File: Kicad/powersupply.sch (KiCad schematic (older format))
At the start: 18 parts, among them J1701 Jack-DC, Q1701 BC546, Q1702 BC556, U1701 DC-DC Module, U1702 MAX1615, U1703 TLV1117 3.3V 1A

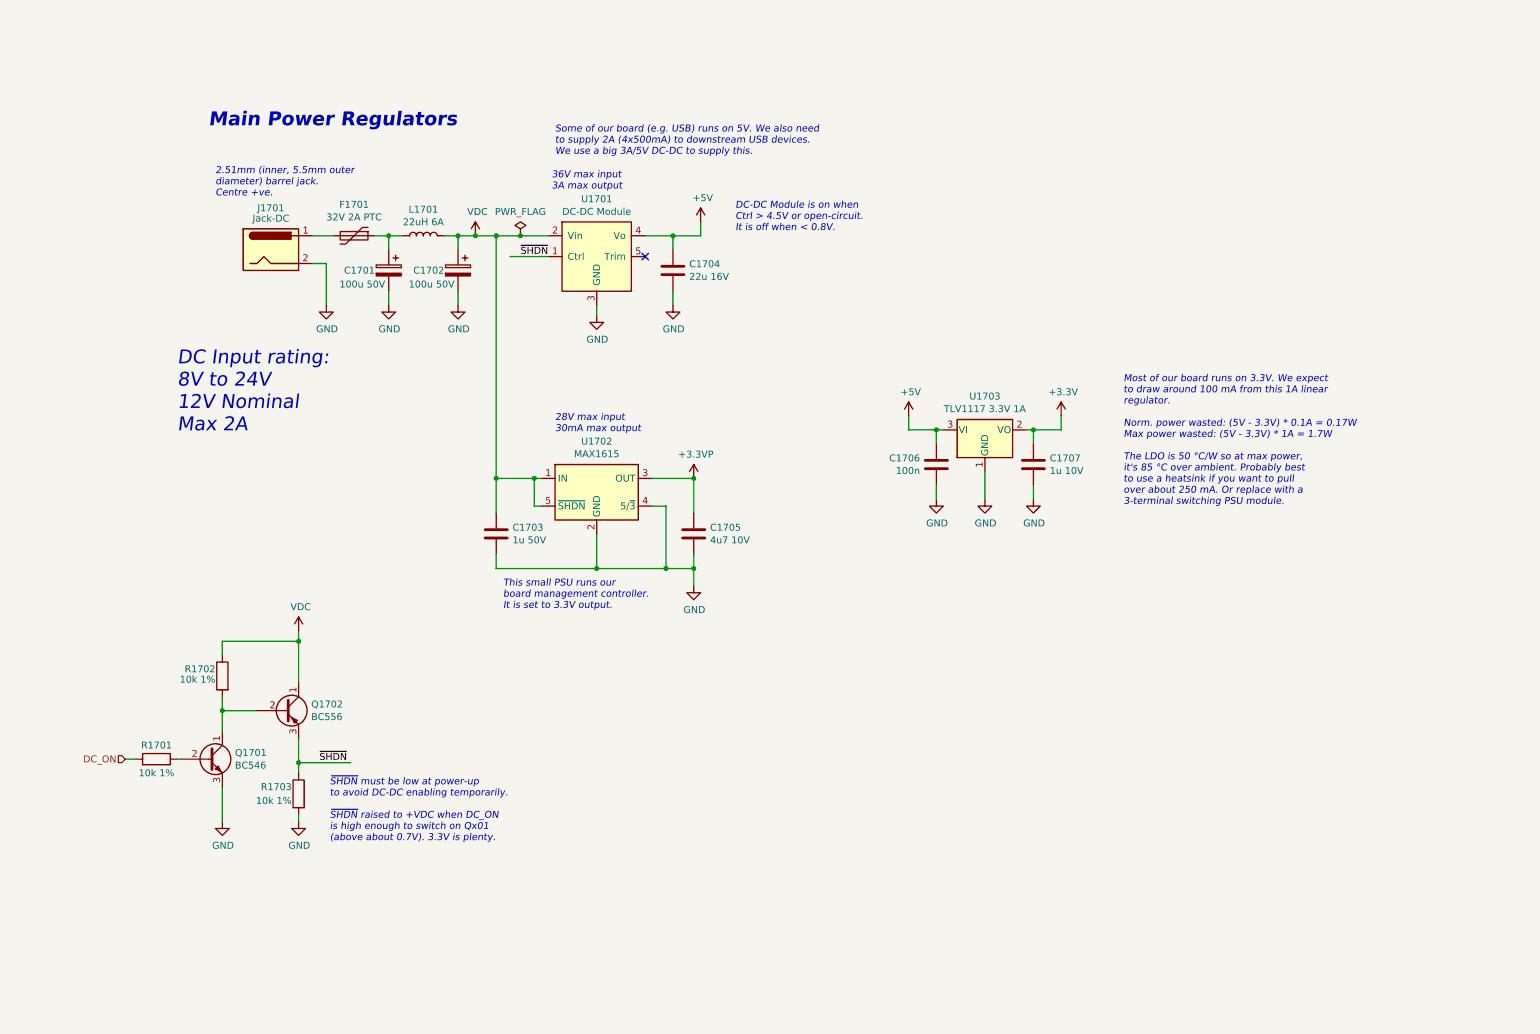
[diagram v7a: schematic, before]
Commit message: Brought in sheets from Neotron Pico.
Also includes DB15HD and PSU 3D models.
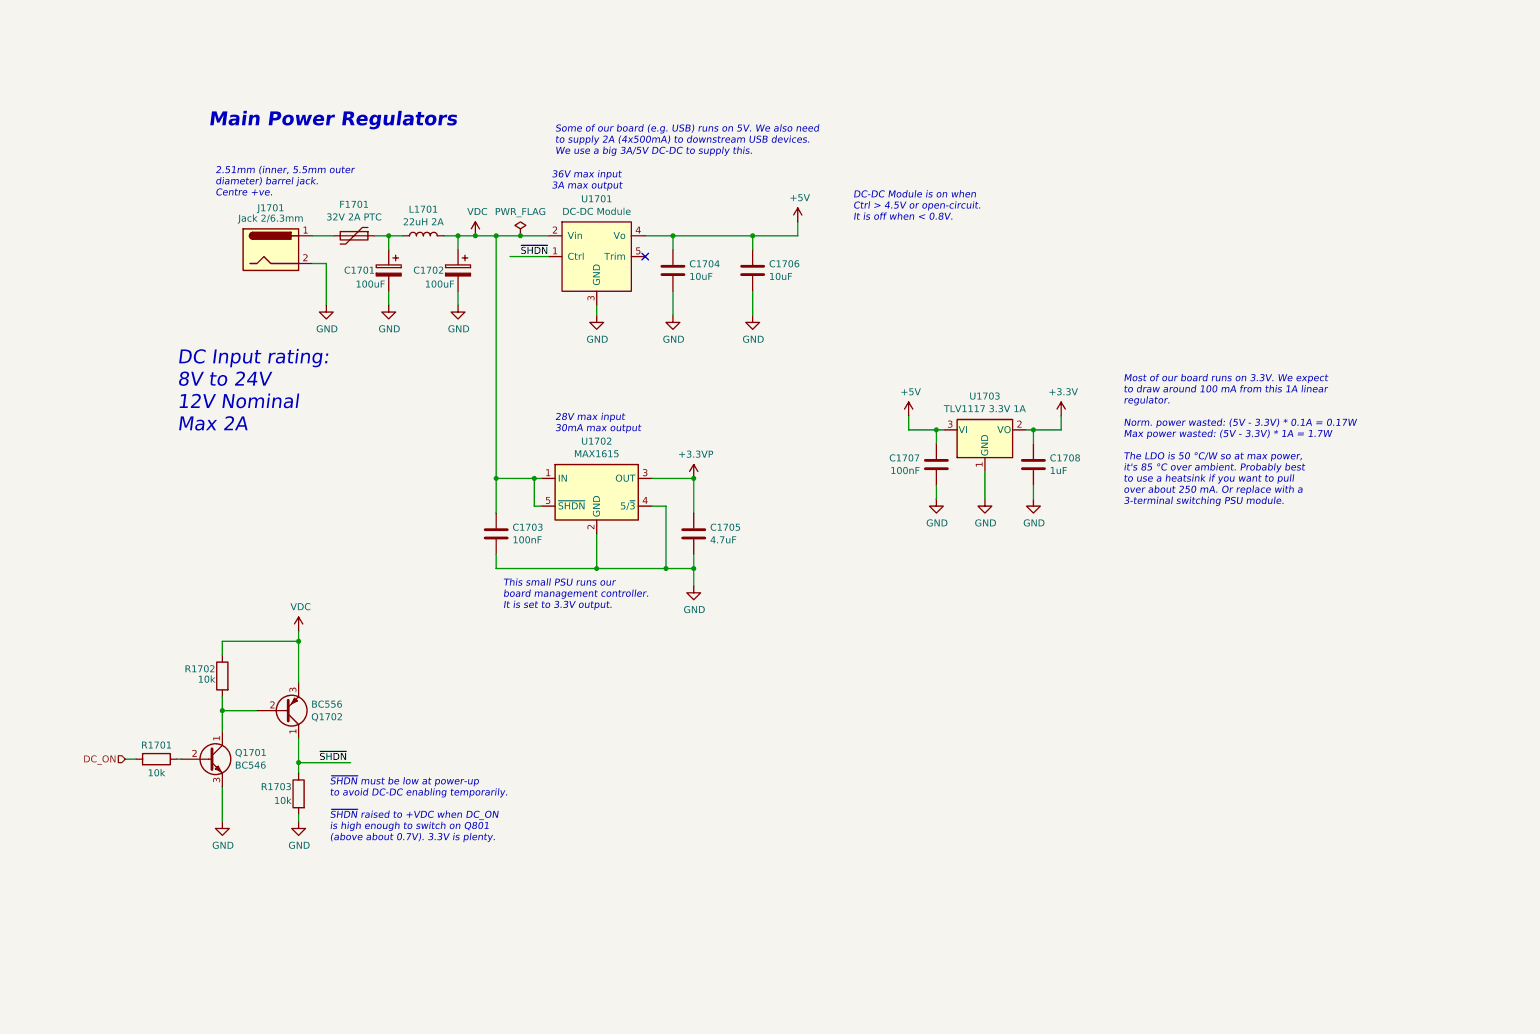
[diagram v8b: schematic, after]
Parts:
- added C1706: 10uF, Capacitor_SMD:C_0805_2012Metric_Pad1.18x1.45mm_HandSolder, symbol Device:C
- C1701, C1702: value 100u 50V -> 100uF; footprint Capacitor_THT:CP_Radial_D6.3mm_P2.50mm -> Capacitor_THT:CP_Radial_D8.0mm_P5.00mm; Digikey 493-5916-1-ND -> (none); MPN UVR1H101MPD1TD -> CPL-CAP-ALU-RAD-100UF-50V; Manufacturer Nichicon -> CPL; Mouser 647-UVR1H101MPD1TD -> (none); Voltage (none) -> 50V
- C1703: value 1u 50V -> 100nF; Digikey 1276-6470-1-ND -> (none); LCSC Part# (none) -> C49678; MPN CL21B105KBFNNNG -> CPL-CAP-X7R-0805-100NF-50V; Manufacturer Samsung -> CPL; Voltage (none) -> 50V
- C1704: value 22u 16V -> 10uF; Digikey 1276-7092-1-ND -> (none); LCSC Part# (none) -> C15850; MPN CL21A226KOQNNNG -> CPL-CAP-X5R-0805-10UF-16V; Manufacturer Samsung -> CPL
- C1705: value 4u7 10V -> 4.7uF; Digikey 1276-6464-1-ND -> (none); LCSC Part# (none) -> C1779; MPN CL21A475KPFNNNG -> CPL-CAP-X5R-0805-4.7UF-25V; Manufacturer Samsung -> CPL
- C1707: renamed from C1706; value 100n -> 100nF; Digikey BC1150CT-ND -> (none); LCSC Part# (none) -> C49678; MPN K104K15X7RF5TL2 -> CPL-CAP-X7R-0805-100NF-50V; Manufacturer Vishay -> CPL; Mouser 594-K104K15X7RF5TL2 -> (none)
- C1708: renamed from C1707; value 1u 10V -> 1uF; Digikey 1276-6471-1-ND -> (none); LCSC Part# (none) -> C28323; MPN CL21B105KOFNNNG -> CPL-CAP-X7R-0805-1UF-25V; Manufacturer Samsung -> CPL
- J1701: value Jack-DC -> Jack 2/6.3mm
- L1701: value 22uH 6A -> 22uH 2A; footprint Inductor_THT:L_Axial_L26.7mm_D12.1mm_P35.00mm_Horizontal_Vishay_IHA-103 -> Inductor_THT:L_Radial_D9.5mm_P5.00mm_Fastron_07HVP; Digikey AIAP-03-220K-ND -> 811-2042-ND; MPN AIAP-03-220K -> 13R223C; Manufacturer Abracon -> Murata; Mouser 815-AIAP03220K -> (none)
- Q1701, Q1702: DNP (none) -> 0
- R1701, R1702, R1703: value 10k 1% -> 10k; Digikey RMCF0805FT10K0-ND -> (none); LCSC Part# (none) -> C17414; MPN RMCF0805FT10K0 -> CPL-RES-0805-10K-0.125W; Manufacturer Stackpole -> CPL
- U1702: LCSC Part# (none) -> C52770
- U1703: LCSC Part# (none) -> C6186; MPN TLV1117LV33DCYR -> CPL-REG-LIN-3.3V-1A; Manufacturer Texas Instruments -> CPL
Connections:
- wire segments 63 -> 66
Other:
- note added: "~SHDN~ must be low at power-up\nto avoid DC-DC enabling temporarily.\n\n~SHDN~ raised to +VDC when DC_ON\nis high enough to switch on Q801\n(above about 0.7V). 3.3V is plenty."
- note removed: "~SHDN~ must be low at power-up\nto avoid DC-DC enabling temporarily.\n\n~SHDN~ raised to +VDC when DC_ON\nis high enough to switch on Qx01\n(above about 0.7V). 3.3V is plenty."
